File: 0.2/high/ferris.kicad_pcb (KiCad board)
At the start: 2 copper layers, 219.1 x 95.2 mm, 109 parts, among them J1 TYPE-C-31-M-12, K0_0 KEYSW, K0_1 KEYSW, K0_2 KEYSW, K0_3 KEYSW, K0_4 KEYSW, K0_5 KEYSW, K0_6 KEYSW, K0_7 KEYSW, K0_8 KEYSW, K0_9 KEYSW, K1_0 KEYSW, K1_1 KEYSW, K1_2 KEYSW, K1_3 KEYSW, K1_4 KEYSW, K1_5 KEYSW, K1_6 KEYSW, K1_7 KEYSW, K1_8 KEYSW, K1_9 KEYSW, K2_0 KEYSW, K2_1 KEYSW, K2_2 KEYSW, K2_3 KEYSW, K2_4 KEYSW, K2_5 KEYSW, K2_6 KEYSW, K2_7 KEYSW, K2_8 KEYSW, K2_9 KEYSW, K3_3 KEYSW, K3_4 KEYSW, K3_5 KEYSW, K3_6 KEYSW, Q1 PDTC123JT,215, SW1 B3U-1000P, U1 STM32F072CBT6, U2 MCP23017-E/SO, U3 MCP1700T-3302E/TT, U4 SRV05-4

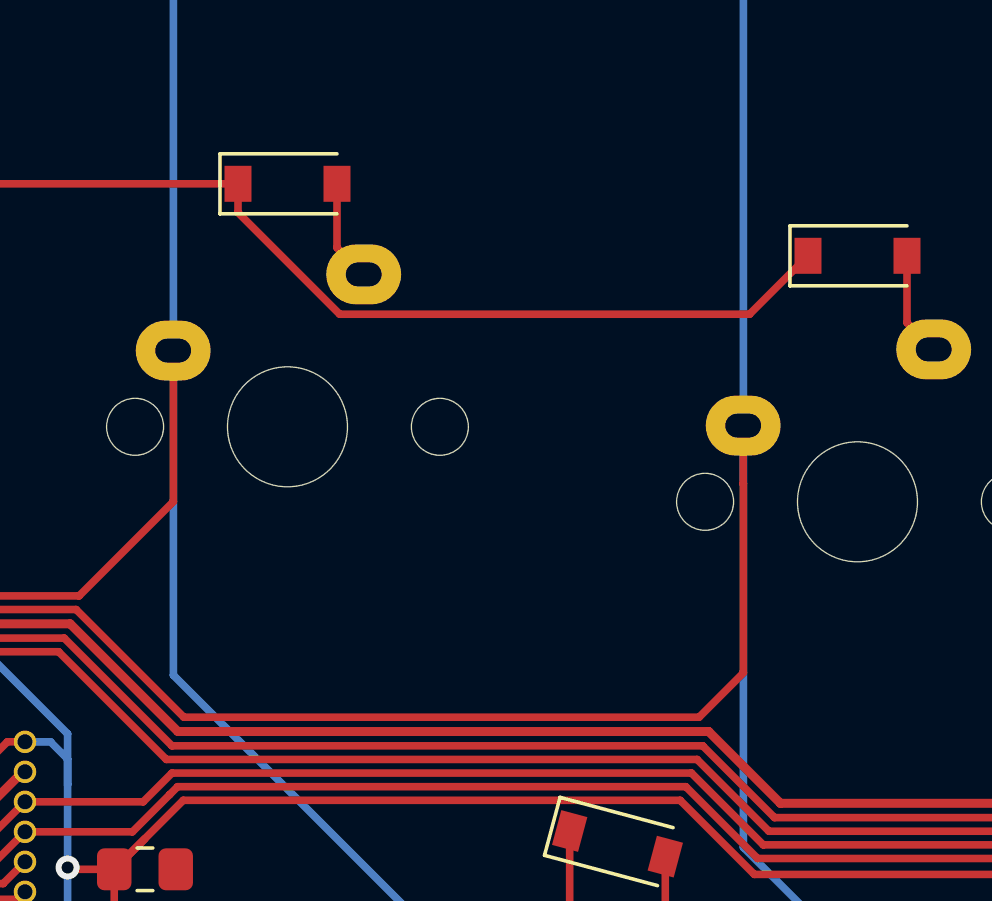
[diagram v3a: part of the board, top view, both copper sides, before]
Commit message: Attempt to replicate fixing hole clearances
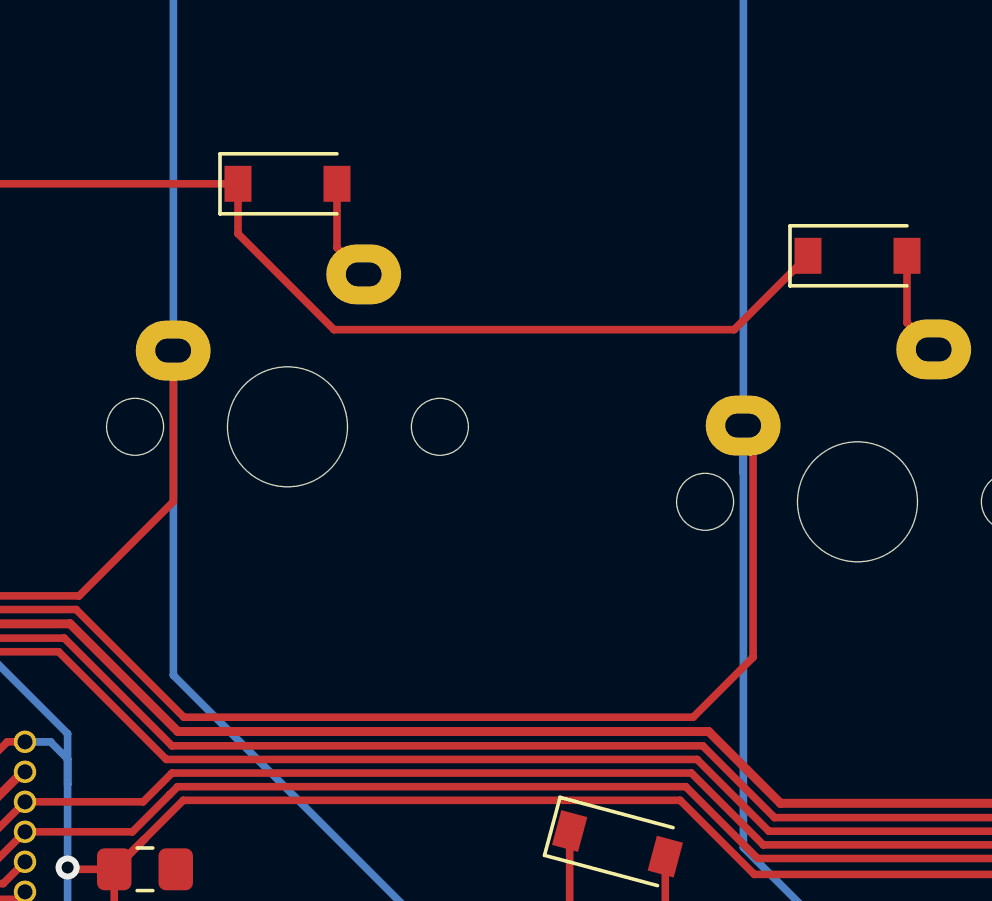
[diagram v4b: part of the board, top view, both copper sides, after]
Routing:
- net /row0,2: track 129.1 -> 130.0 mm
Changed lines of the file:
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@@
   (segment (start 114.885012 67.27499) (end 111.75501 67.27499) (width 0.3) (layer "F.Cu") (net 2))
   (segment (start 115.245 65.254998) (end 115.245 66.06) (width 0.3) (layer "F.Cu") (net 2))
+  (segment (start 96.52 67.79) (end 96.52 67.818) (width 0.254) (layer "F.Cu") (net 3))
+  (segment (start 56.82299 71.810992) (end 56.82299 77.57299) (width 0.254) (layer "F.Cu") (net 3))
   (segment (start 57.8375 78) (end 57.25 78) (width 0.254) (layer "F.Cu") (net 3))
+  (segment (start 94.524145 77.179855) (end 77.544136 77.179855) (width 0.254) (layer "F.Cu") (net 3))
+  (segment (start 67.149969 73.589969) (end 64.532981 70.972981) (width 0.254) (layer "F.Cu") (net 3))
+  (segment (start 56.82299 77.57299) (end 57.25 78) (width 0.254) (layer "F.Cu") (net 3))
+  (segment (start 96.19 67.46) (end 96.52 67.79) (width 0.254) (layer "F.Cu") (net 3))
+  (segment (start 96.52 75.184) (end 94.524145 77.179855) (width 0.254) (layer "F.Cu") (net 3))
+  (segment (start 73.954255 73.589969) (end 67.149969 73.589969) (width 0.254) (layer "F.Cu") (net 3))
+  (segment (start 57.661001 70.972981) (end 56.82299 71.810992) (width 0.254) (layer "F.Cu") (net 3))
+  (segment (start 96.52 67.818) (end 96.52 75.184) (width 0.254) (layer "F.Cu") (net 3))
+  (segment (start 60.5875 80.75) (end 57.8375 78) (width 0.254) (layer "F.Cu") (net 3))
   (segment (start 64.532981 70.972981) (end 57.661001 70.972981) (width 0.254) (layer "F.Cu") (net 3))
-  (segment (start 56.82299 77.57299) (end 57.25 78) (width 0.254) (layer "F.Cu") (net 3))
-  (segment (start 56.82299 71.810992) (end 56.82299 77.57299) (width 0.254) (layer "F.Cu") (net 3))
-  (segment (start 96.197001 75.702709) (end 94.719855 77.179855) (width 0.254) (layer "F.Cu") (net 3))
-  (segment (start 96.19 67.46) (end 96.19 69.380038) (width 0.254) (layer "F.Cu") (net 3))
-  (segment (start 57.661001 70.972981) (end 56.82299 71.810992) (width 0.254) (layer "F.Cu") (net 3))
-  (segment (start 96.19 69.380038) (end 96.197001 69.387039) (width 0.254) (layer "F.Cu") (net 3))
-  (segment (start 73.954255 73.589969) (end 67.149969 73.589969) (width 0.254) (layer "F.Cu") (net 3))
-  (segment (start 67.149969 73.589969) (end 64.532981 70.972981) (width 0.254) (layer "F.Cu") (net 3))
-  (segment (start 60.5875 80.75) (end 57.8375 78) (width 0.254) (layer "F.Cu") (net 3))
-  (segment (start 94.719855 77.179855) (end 77.544136 77.179855) (width 0.254) (layer "F.Cu") (net 3))
   (segment (start 77.544136 77.179855) (end 73.954255 73.589969) (width 0.254) (layer "F.Cu") (net 3))
-  (segment (start 96.197001 69.387039) (end 96.197001 75.702709) (width 0.254) (layer "F.Cu") (net 3))
   (segment (start 96.197001 29.467001) (end 96.197001 48.452999) (width 0.254) (layer "B.Cu") (net 3))
   (segment (start 96.19 48.46) (end 96.197001 48.467001) (width 0.254) (layer "B.Cu") (net 3))
@@
   (segment (start 60.35 54.856675) (end 64.893325 59.4) (width 0.254) (layer "F.Cu") (net 19))
   (segment (start 60.5875 82.75) (end 58 82.75) (width 0.254) (layer "F.Cu") (net 19))
+  (segment (start 79.35 61.062) (end 82.55 64.262) (width 0.254) (layer "F.Cu") (net 19))
+  (segment (start 95.888 64.262) (end 98.35 61.8) (width 0.254) (layer "F.Cu") (net 19))
   (segment (start 47.35 53.8) (end 60.35 53.8) (width 0.254) (layer "F.Cu") (net 19))
   (segment (start 45.179971 70.781011) (end 38.391049 70.781011) (width 0.254) (layer "F.Cu") (net 19))
+  (segment (start 82.55 64.262) (end 95.888 64.262) (width 0.254) (layer "F.Cu") (net 19))
   (segment (start 22.35 71.8) (end 34.35 59.8) (width 0.254) (layer "F.Cu") (net 19))
   (segment (start 56.39896 82) (end 45.179971 70.781011) (width 0.254) (layer "F.Cu") (net 19))
@@
   (segment (start 64.893325 59.4) (end 79.35 59.4) (width 0.254) (layer "F.Cu") (net 19))
   (segment (start 60.35 53.8) (end 60.35 54.856675) (width 0.254) (layer "F.Cu") (net 19))
-  (segment (start 96.40299 63.74701) (end 98.35 61.8) (width 0.254) (layer "F.Cu") (net 19))
-  (segment (start 82.740335 63.74701) (end 96.40299 63.74701) (width 0.254) (layer "F.Cu") (net 19))
+  (segment (start 79.35 59.4) (end 79.35 61.062) (width 0.254) (layer "F.Cu") (net 19))
   (segment (start 58 82.75) (end 57.25 82) (width 0.254) (layer "F.Cu") (net 19))
   (segment (start 41.35 59.8) (end 47.35 53.8) (width 0.254) (layer "F.Cu") (net 19))
-  (segment (start 79.35 59.4) (end 79.35 60.356675) (width 0.254) (layer "F.Cu") (net 19))
-  (segment (start 79.35 60.356675) (end 82.740335 63.74701) (width 0.254) (layer "F.Cu") (net 19))
   (segment (start 87.01299 89.72299) (end 87.01299 88.543048) (width 0.254) (layer "F.Cu") (net 20))
   (segment (start 87.01299 88.543048) (end 90.406222 85.149816) (width 0.254) (layer "F.Cu") (net 20))
